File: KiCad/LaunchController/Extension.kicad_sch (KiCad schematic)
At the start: 15 parts, among them J10 CONN_EXT_I2C_2, J11 CONN_EXT_I2C_3, J12 CONN_EXT_SPI_0, J13 CONN_EXT_SPI_1, J14 CONN_EXT_SPI_2, J17 CONN_EXT_GPIO_0, J18 CONN_EXT_GPIO_1, J19 CONN_EXT_GPIO_2, J20 CONN_EXT_GPIO_3, J7 CONN_EXT_UART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

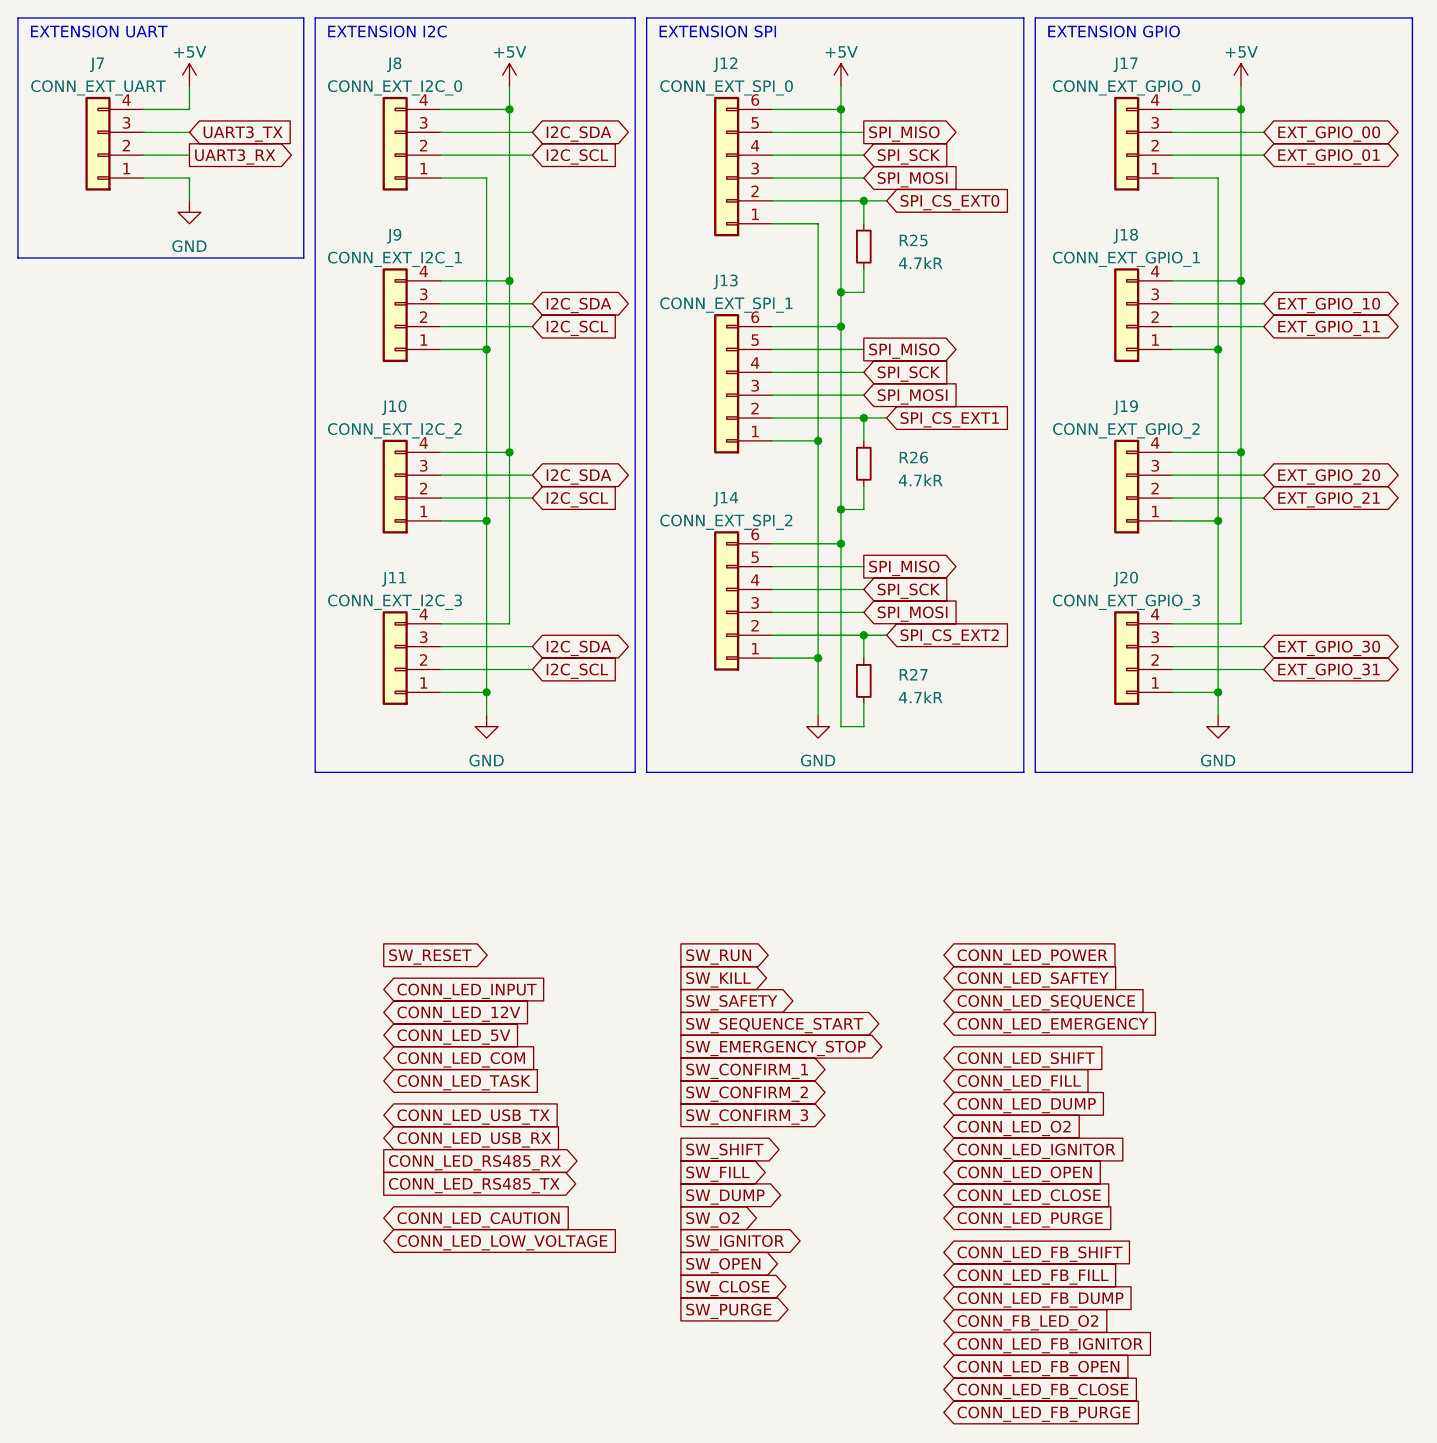
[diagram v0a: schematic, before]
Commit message: 端子台を選定
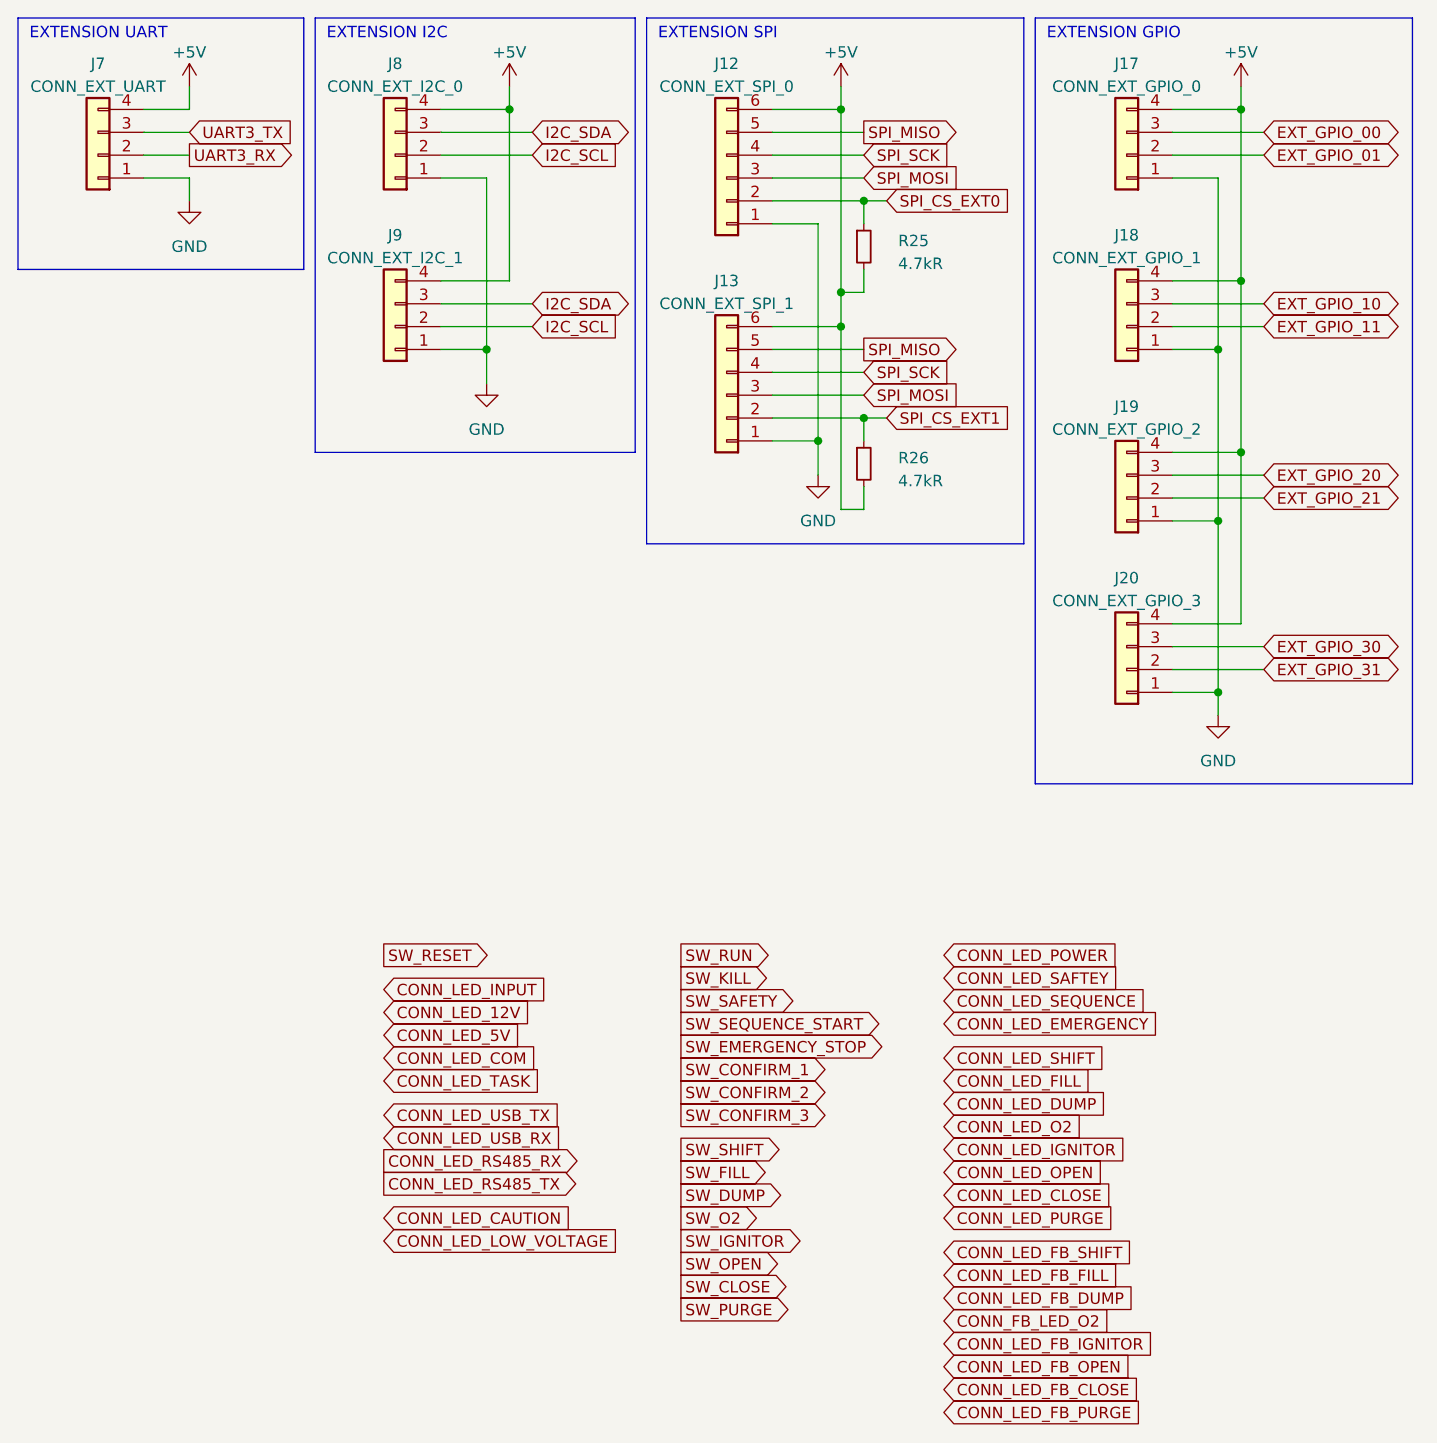
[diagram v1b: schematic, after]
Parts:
- removed J10: CONN_EXT_I2C_2, Connector_JST:JST_XH_B4B-XH-A_1x04_P2.50mm_Vertical, symbol Connector_Generic:Conn_01x04
- removed J11: CONN_EXT_I2C_3, Connector_JST:JST_XH_B4B-XH-A_1x04_P2.50mm_Vertical, symbol Connector_Generic:Conn_01x04
- removed J14: CONN_EXT_SPI_2, Connector_JST:JST_XH_B6B-XH-A_1x06_P2.50mm_Vertical, symbol Connector_Generic:Conn_01x06
- removed R27: 4.7kR, Resistor_SMD:R_0603_1608Metric_Pad0.98x0.95mm_HandSolder, symbol Device:R_Small

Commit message: 拡張スロットを削除
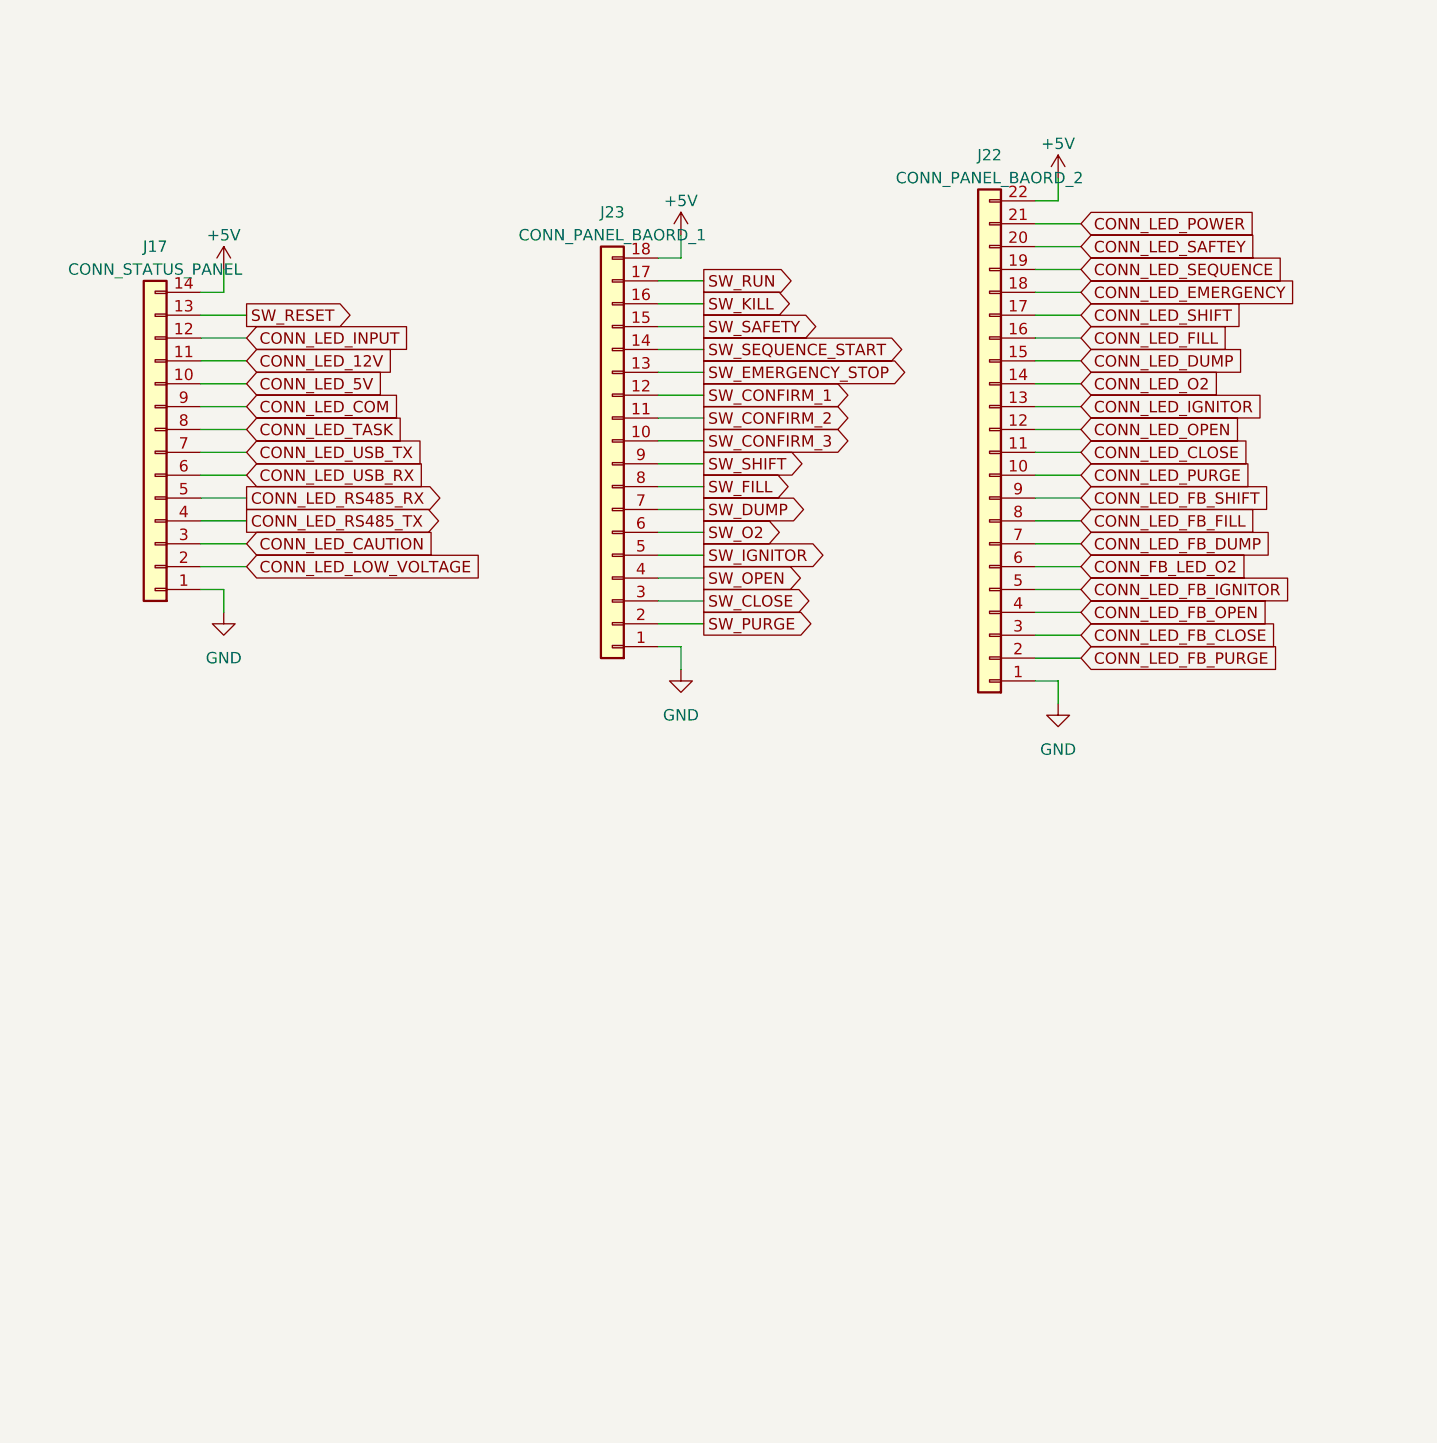
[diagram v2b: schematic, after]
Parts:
- removed J12: CONN_EXT_SPI_0, Connector_JST:JST_XH_B6B-XH-A_1x06_P2.50mm_Vertical, symbol Connector_Generic:Conn_01x06
- removed J13: CONN_EXT_SPI_1, Connector_JST:JST_XH_B6B-XH-A_1x06_P2.50mm_Vertical, symbol Connector_Generic:Conn_01x06
- removed J17: CONN_EXT_GPIO_0, Connector_JST:JST_XH_B4B-XH-A_1x04_P2.50mm_Vertical, symbol Connector_Generic:Conn_01x04
- removed J18: CONN_EXT_GPIO_1, Connector_JST:JST_XH_B4B-XH-A_1x04_P2.50mm_Vertical, symbol Connector_Generic:Conn_01x04
- removed J19: CONN_EXT_GPIO_2, Connector_JST:JST_XH_B4B-XH-A_1x04_P2.50mm_Vertical, symbol Connector_Generic:Conn_01x04
- removed J20: CONN_EXT_GPIO_3, Connector_JST:JST_XH_B4B-XH-A_1x04_P2.50mm_Vertical, symbol Connector_Generic:Conn_01x04
- removed J7: CONN_EXT_UART, Connector_JST:JST_XH_B4B-XH-A_1x04_P2.50mm_Vertical, symbol Connector_Generic:Conn_01x04
- removed J8: CONN_EXT_I2C_0, Connector_JST:JST_XH_B4B-XH-A_1x04_P2.50mm_Vertical, symbol Connector_Generic:Conn_01x04
- removed J9: CONN_EXT_I2C_1, Connector_JST:JST_XH_B4B-XH-A_1x04_P2.50mm_Vertical, symbol Connector_Generic:Conn_01x04
- removed R25, R26: 4.7kR, Resistor_SMD:R_0603_1608Metric_Pad0.98x0.95mm_HandSolder, symbol Device:R_Small
- added J17: CONN_STATUS_PANEL, TSRP_Connector_Hirose:DF51A-14DP-2DS, symbol Connector_Generic:Conn_01x14
- added J22: CONN_PANEL_BAORD_2, TSRP_Connector_Hirose:DF51A-22DP-2DS, symbol Connector_Generic:Conn_01x22
- added J23: CONN_PANEL_BAORD_1, TSRP_Connector_Hirose:DF51A-18DP-2DS, symbol Connector_Generic:Conn_01x18
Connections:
- net +5V: now also J17.14 (Pin_14), J22.22 (Pin_22), J23.18 (Pin_18)
- net CONN_FB_LED_O2: now also J22.6 (Pin_6)
- net CONN_LED_12V: now also J17.11 (Pin_11)
- net CONN_LED_5V: now also J17.10 (Pin_10)
- net CONN_LED_CAUTION: now also J17.3 (Pin_3)
- net CONN_LED_CLOSE: now also J22.11 (Pin_11)
- net CONN_LED_COM: now also J17.9 (Pin_9)
- net CONN_LED_DUMP: now also J22.15 (Pin_15)
- net CONN_LED_EMERGENCY: now also J22.18 (Pin_18)
- net CONN_LED_FB_CLOSE: now also J22.3 (Pin_3)
- net CONN_LED_FB_DUMP: now also J22.7 (Pin_7)
- net CONN_LED_FB_FILL: now also J22.8 (Pin_8)
- net CONN_LED_FB_IGNITOR: now also J22.5 (Pin_5)
- net CONN_LED_FB_OPEN: now also J22.4 (Pin_4)
- net CONN_LED_FB_PURGE: now also J22.2 (Pin_2)
- net CONN_LED_FB_SHIFT: now also J22.9 (Pin_9)
- net CONN_LED_FILL: now also J22.16 (Pin_16)
- net CONN_LED_IGNITOR: now also J22.13 (Pin_13)
- net CONN_LED_INPUT: now also J17.12 (Pin_12)
- net CONN_LED_LOW_VOLTAGE: now also J17.2 (Pin_2)
- net CONN_LED_O2: now also J22.14 (Pin_14)
- net CONN_LED_OPEN: now also J22.12 (Pin_12)
- net CONN_LED_POWER: now also J22.21 (Pin_21)
- net CONN_LED_PURGE: now also J22.10 (Pin_10)
- net CONN_LED_RS485_RX: now also J17.5 (Pin_5)
- net CONN_LED_RS485_TX: now also J17.4 (Pin_4)
- net CONN_LED_SAFTEY: now also J22.20 (Pin_20)
- net CONN_LED_SEQUENCE: now also J22.19 (Pin_19)
- net CONN_LED_SHIFT: now also J22.17 (Pin_17)
- net CONN_LED_TASK: now also J17.8 (Pin_8)
- net CONN_LED_USB_RX: now also J17.6 (Pin_6)
- net CONN_LED_USB_TX: now also J17.7 (Pin_7)
- net GND: now also J17.1 (Pin_1), J22.1 (Pin_1), J23.1 (Pin_1)
- net SW_CLOSE: now also J23.3 (Pin_3)
- net SW_CONFIRM_1: now also J23.12 (Pin_12)
- net SW_CONFIRM_2: now also J23.11 (Pin_11)
- net SW_CONFIRM_3: now also J23.10 (Pin_10)
- net SW_DUMP: now also J23.7 (Pin_7)
- net SW_EMERGENCY_STOP: now also J23.13 (Pin_13)
- net SW_FILL: now also J23.8 (Pin_8)
- net SW_IGNITOR: now also J23.5 (Pin_5)
- net SW_KILL: now also J23.16 (Pin_16)
- net SW_O2: now also J23.6 (Pin_6)
- net SW_OPEN: now also J23.4 (Pin_4)
- net SW_PURGE: now also J23.2 (Pin_2)
- net SW_RESET: now also J17.13 (Pin_13)
- net SW_RUN: now also J23.17 (Pin_17)
- net SW_SAFETY: now also J23.15 (Pin_15)
- net SW_SEQUENCE_START: now also J23.14 (Pin_14)
- net SW_SHIFT: now also J23.9 (Pin_9)
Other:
- note removed: "EXTENSION GPIO"
- note removed: "EXTENSION I2C"
- note removed: "EXTENSION SPI"
- note removed: "EXTENSION UART"

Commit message: 配線終わらん
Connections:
- net CONN_LED_CLOSE renamed LED_CLOSE
- net CONN_LED_DUMP renamed LED_DUMP
- net CONN_LED_FB_SHIFT renamed LED_FB_SHIFT
- net CONN_LED_IGNITOR renamed LED_IGNITOR
- net CONN_LED_POWER renamed LED_POWER
- net CONN_LED_SAFTEY renamed LED_SAFTEY
- net CONN_LED_SEQUENCE renamed LED_SEQUENCE
- net CONN_LED_SHIFT renamed LED_SHIFT
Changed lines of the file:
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@@
     )
   )
-  (global_label "CONN_LED_SEQUENCE" (shape input) (at 130.81 40.64 0) (fields_autoplaced)
+  (global_label "LED_SEQUENCE" (shape input) (at 130.81 40.64 0) (fields_autoplaced)
     (effects (font (size 1.27 1.27)) (justify left))
-    (property "Intersheetrefs" "${INTERSHEET_REFS}" (at 154.2776 40.64 0)
+    (property "Intersheetrefs" "${INTERSHEET_REFS}" (at 148.0485 40.64 0)
       (effects (font (size 1.27 1.27)) (justify left) hide)
     )
   )
-  (global_label "CONN_LED_SAFTEY" (shape input) (at 130.81 38.1 0) (fields_autoplaced)
+  (global_label "LED_SAFTEY" (shape input) (at 130.81 38.1 0) (fields_autoplaced)
     (effects (font (size 1.27 1.27)) (justify left))
-    (property "Intersheetrefs" "${INTERSHEET_REFS}" (at 150.9515 38.1 0)
+    (property "Intersheetrefs" "${INTERSHEET_REFS}" (at 144.7224 38.1 0)
       (effects (font (size 1.27 1.27)) (justify left) hide)
     )
@@
     )
   )
-  (global_label "CONN_LED_FB_SHIFT" (shape input) (at 130.81 66.04 0) (fields_autoplaced)
+  (global_label "LED_FB_SHIFT" (shape input) (at 130.81 66.04 0) (fields_autoplaced)
     (effects (font (size 1.27 1.27)) (justify left))
-    (property "Intersheetrefs" "${INTERSHEET_REFS}" (at 152.8868 66.04 0)
+    (property "Intersheetrefs" "${INTERSHEET_REFS}" (at 146.6577 66.04 0)
       (effects (font (size 1.27 1.27)) (justify left) hide)
     )
@@
     )
   )
-  (global_label "CONN_LED_POWER" (shape input) (at 130.81 35.56 0) (fields_autoplaced)
+  (global_label "LED_POWER" (shape input) (at 130.81 35.56 0) (fields_autoplaced)
     (effects (font (size 1.27 1.27)) (justify left))
-    (property "Intersheetrefs" "${INTERSHEET_REFS}" (at 150.8305 35.56 0)
+    (property "Intersheetrefs" "${INTERSHEET_REFS}" (at 144.6014 35.56 0)
       (effects (font (size 1.27 1.27)) (justify left) hide)
     )
   )
-  (global_label "CONN_LED_IGNITOR" (shape input) (at 130.81 55.88 0) (fields_autoplaced)
+  (global_label "LED_IGNITOR" (shape input) (at 130.81 55.88 0) (fields_autoplaced)
     (effects (font (size 1.27 1.27)) (justify left))
-    (property "Intersheetrefs" "${INTERSHEET_REFS}" (at 151.7378 55.88 0)
+    (property "Intersheetrefs" "${INTERSHEET_REFS}" (at 145.5087 55.88 0)
       (effects (font (size 1.27 1.27)) (justify left) hide)
     )
@@
     )
   )
-  (global_label "CONN_LED_SHIFT" (shape input) (at 130.81 45.72 0) (fields_autoplaced)
+  (global_label "LED_SHIFT" (shape input) (at 130.81 45.72 0) (fields_autoplaced)
     (effects (font (size 1.27 1.27)) (justify left))
-    (property "Intersheetrefs" "${INTERSHEET_REFS}" (at 149.5606 45.72 0)
+    (property "Intersheetrefs" "${INTERSHEET_REFS}" (at 143.3315 45.72 0)
       (effects (font (size 1.27 1.27)) (justify left) hide)
     )
@@
     )
   )
-  (global_label "CONN_LED_DUMP" (shape input) (at 130.81 50.8 0) (fields_autoplaced)
+  (global_label "LED_DUMP" (shape input) (at 130.81 50.8 0) (fields_autoplaced)
     (effects (font (size 1.27 1.27)) (justify left))
-    (property "Intersheetrefs" "${INTERSHEET_REFS}" (at 149.6815 50.8 0)
+    (property "Intersheetrefs" "${INTERSHEET_REFS}" (at 143.4524 50.8 0)
       (effects (font (size 1.27 1.27)) (justify left) hide)
     )
@@
     )
   )
-  (global_label "CONN_LED_CLOSE" (shape input) (at 130.81 60.96 0) (fields_autoplaced)
+  (global_label "LED_CLOSE" (shape input) (at 130.81 60.96 0) (fields_autoplaced)
     (effects (font (size 1.27 1.27)) (justify left))
-    (property "Intersheetrefs" "${INTERSHEET_REFS}" (at 150.3467 60.96 0)
+    (property "Intersheetrefs" "${INTERSHEET_REFS}" (at 144.1176 60.96 0)
       (effects (font (size 1.27 1.27)) (justify left) hide)
     )
